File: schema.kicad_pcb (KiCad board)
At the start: 2 copper layers, 43.7 x 40.5 mm, 7 parts, among them U1 74HC595D, U2 74HC595D, U5 AT28C256-15PU

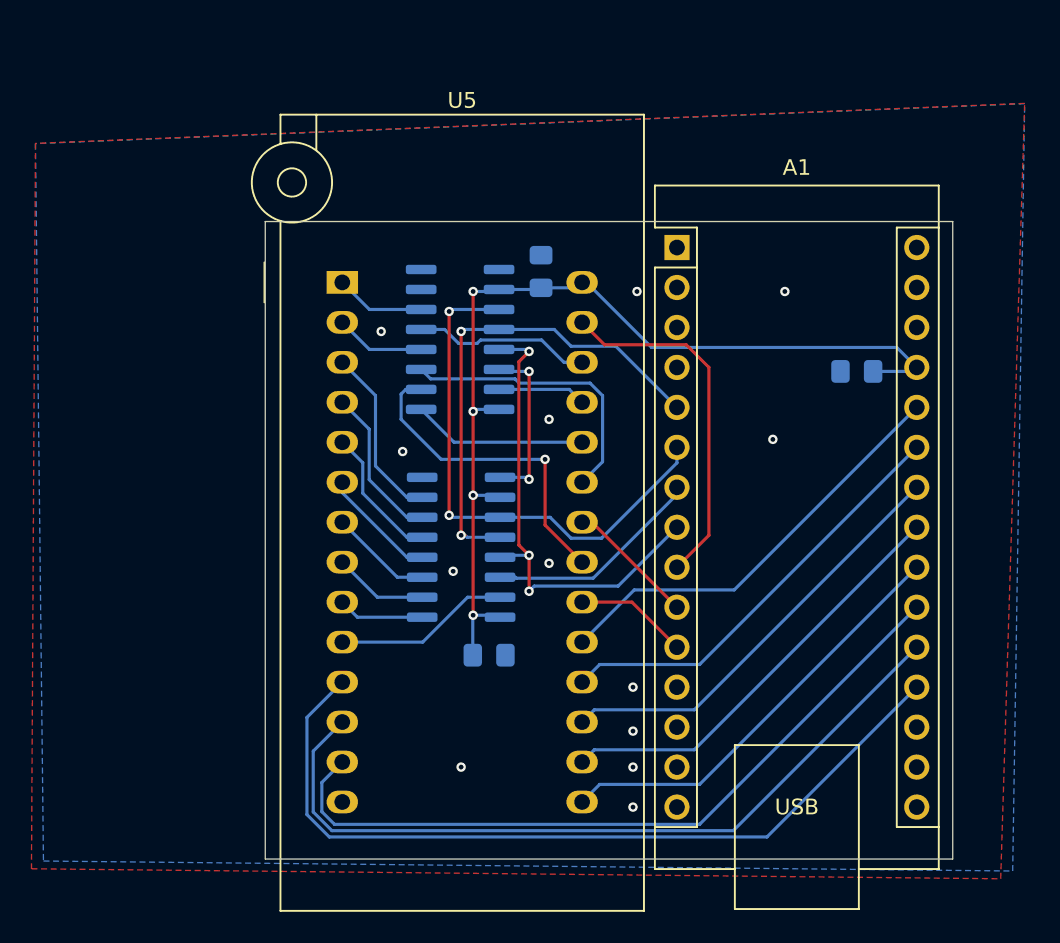
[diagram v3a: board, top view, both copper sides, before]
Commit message: change pinout
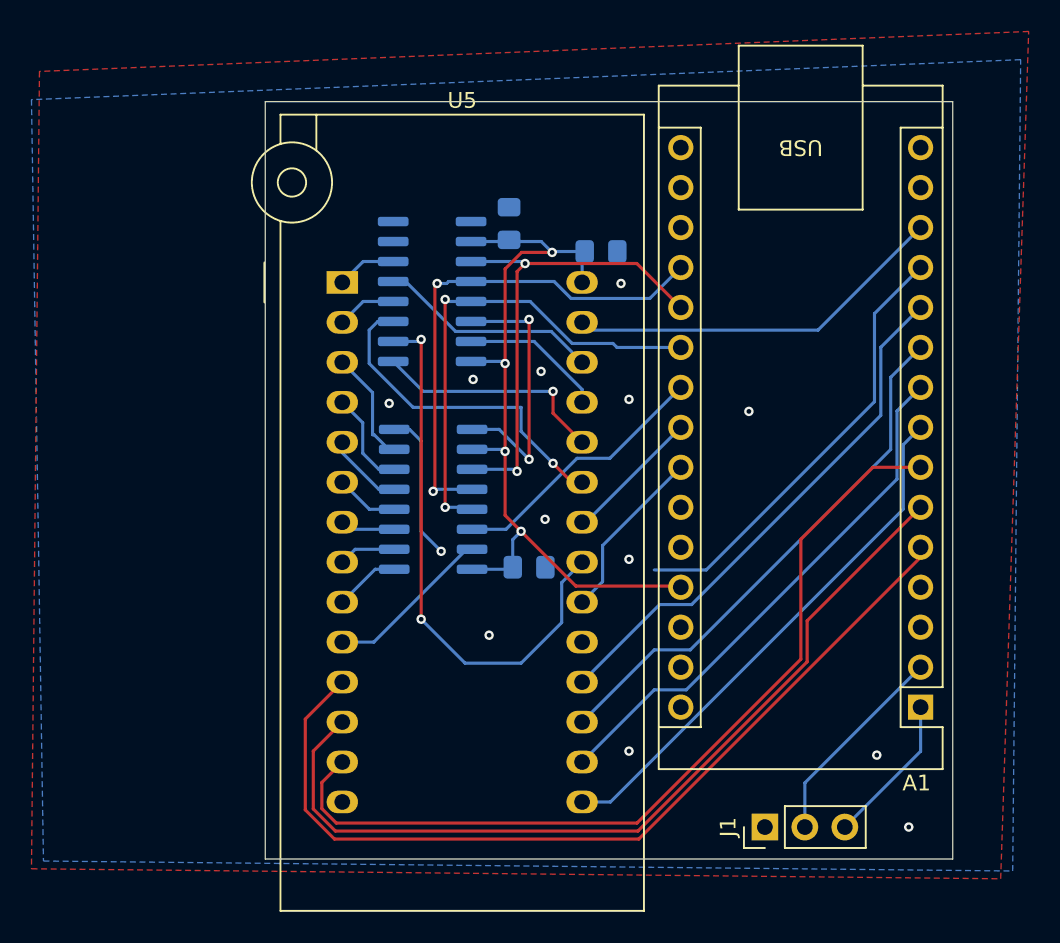
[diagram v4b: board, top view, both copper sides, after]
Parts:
- added J1: Conn_01x03, Connector_PinHeader_2.54mm:PinHeader_1x03_P2.54mm_Vertical, F.Cu at (152.4, 119.6)
- moved A1 33.1 mm to (162.3, 112.0), turned to 180 degrees
- moved C3 26.6 mm to (142.0, 83.1)
- moved C2 24.3 mm to (137.4, 103.1), turned to 0 degrees
- moved C1 3.66 mm to (136.1, 81.3)
- moved U2 3.53 mm to (131.3, 85.6)
- moved U1 3.53 mm to (131.3, 98.8)
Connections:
- A1 pad 1: unconnected-(A1-TX1-Pad1) -> Net-(A1-TX1)
- A1 pad 10: Net-(A1-D7) -> /D5
- A1 pad 11: Net-(A1-D8) -> /D6
- A1 pad 12: unconnected-(A1-D9-Pad12) -> /D7
- A1 pad 13: unconnected-(A1-D10-Pad13) -> Net-(A1-D10)
- A1 pad 19: /D0 -> Net-(A1-A0)
- A1 pad 2: unconnected-(A1-RX1-Pad2) -> Net-(A1-RX1)
- A1 pad 20: /D1 -> Net-(A1-A1)
- A1 pad 21: /D2 -> Net-(A1-A2)
- A1 pad 22: /D3 -> Net-(A1-A3)
- A1 pad 23: /D4 -> Net-(A1-SDA/A4)
- A1 pad 24: /D5 -> Net-(A1-SCL/A5)
- A1 pad 25: /D6 -> unconnected-(A1-A6-Pad25)
- A1 pad 26: /D7 -> unconnected-(A1-A7-Pad26)
- A1 pad 5: Net-(A1-D2) -> /D0
- A1 pad 6: Net-(A1-D3) -> /D1
- A1 pad 7: Net-(A1-D4) -> /D2
- A1 pad 8: Net-(A1-D5) -> /D3
- A1 pad 9: Net-(A1-D6) -> /D4
- U1 pad 11: Net-(A1-D3) -> Net-(A1-A1)
- U1 pad 12: Net-(A1-D2) -> Net-(A1-A0)
- U1 pad 13: Net-(A1-D5) -> Net-(A1-A2)
- U1 pad 14: Net-(A1-D4) -> Net-(A1-A3)
- U2 pad 11: Net-(A1-D3) -> Net-(A1-A1)
- U2 pad 12: Net-(A1-D2) -> Net-(A1-A0)
- U2 pad 13: Net-(A1-D5) -> Net-(A1-A2)
- U5 pad 20: Net-(A1-D8) -> Net-(A1-SCL/A5)
- U5 pad 22: Net-(A1-D7) -> Net-(A1-SDA/A4)
- U5 pad 27: Net-(A1-D6) -> Net-(A1-D10)
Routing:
- net Net-(A1-D3): track 34.2 -> 0.00 mm, vias 2 -> 0
- net Net-(A1-A0): track 0.00 -> 32.6 mm, vias 0 -> 2
- net Net-(A1-A2): track 0.00 -> 31.2 mm, vias 0 -> 2
- net Net-(A1-D2): track 31.2 -> 0.00 mm, vias 2 -> 0
- net Net-(A1-A1): track 0.00 -> 30.9 mm, vias 0 -> 2
- net Net-(A1-D5): track 30.7 -> 0.00 mm, vias 3 -> 0
- net Net-(A1-D10): track 0.00 -> 24.4 mm
- net Net-(A1-D6): track 22.8 -> 0.00 mm
- net Net-(A1-A3): track 0.00 -> 17.0 mm
- net /A10: track 20.7 -> 35.1 mm, vias 1 -> 2
- net Net-(A1-D4): track 13.9 -> 0.00 mm
- net Net-(A1-RX1): track 0.00 -> 13.2 mm
- net +5VD: track 62.6 -> 51.3 mm
- net Net-(A1-SCL/A5): track 0.00 -> 11.2 mm
- net Net-(A1-TX1): track 0.00 -> 9.61 mm
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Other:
- board size 43.7 x 40.5 mm -> 43.7 x 48.1 mm
